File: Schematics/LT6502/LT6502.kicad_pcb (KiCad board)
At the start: 4 copper layers, 261 x 83 mm, 227 parts, among them IC1 ATF1508AS-7AX100, IC2 MP2636GR-P, IC3 W65C22S6TQG-14, J1 Conn_02x05_Odd_Even, J11 Conn_02x04_Odd_Even, J12 Conn_02x06_Odd_Even, J13 Conn_02x06_Odd_Even, J14 KeyConn, J15 Conn_01x06, J16 Conn_01x03, J18 Conn_01x03, J2 USBPD_PROG, J3 USB_C_Receptacle_USB2.0_16P, J4 BATTERY JST PH-2A, J5 Conn_02x20_Odd_Even, J6 USB_C_Receptacle_USB2.0_16P, J7 Conn_01x02, J8 Conn_02x26_Top_Bottom, J9 DIN41612_02x32_AC, Q1 STL9P3LLH6, Q2 IRLML6402, Q3 STL9P3LLH6, U1 TC1232, U10 FT245RNL, U11 LM386, U12 W65C51NxP, U2 W65C02S6TQG-14, U3 IS62C256AL, U4 IS62C256AL, U5 SST39SF010, U6 STUSB4500QTR, U7 AP63203WU, U8 TXS0108, U9 TXS0108, X1 28.322MHz, X2 1.8432MHz, Y1 ECS-P55-28.000MHZ-AN

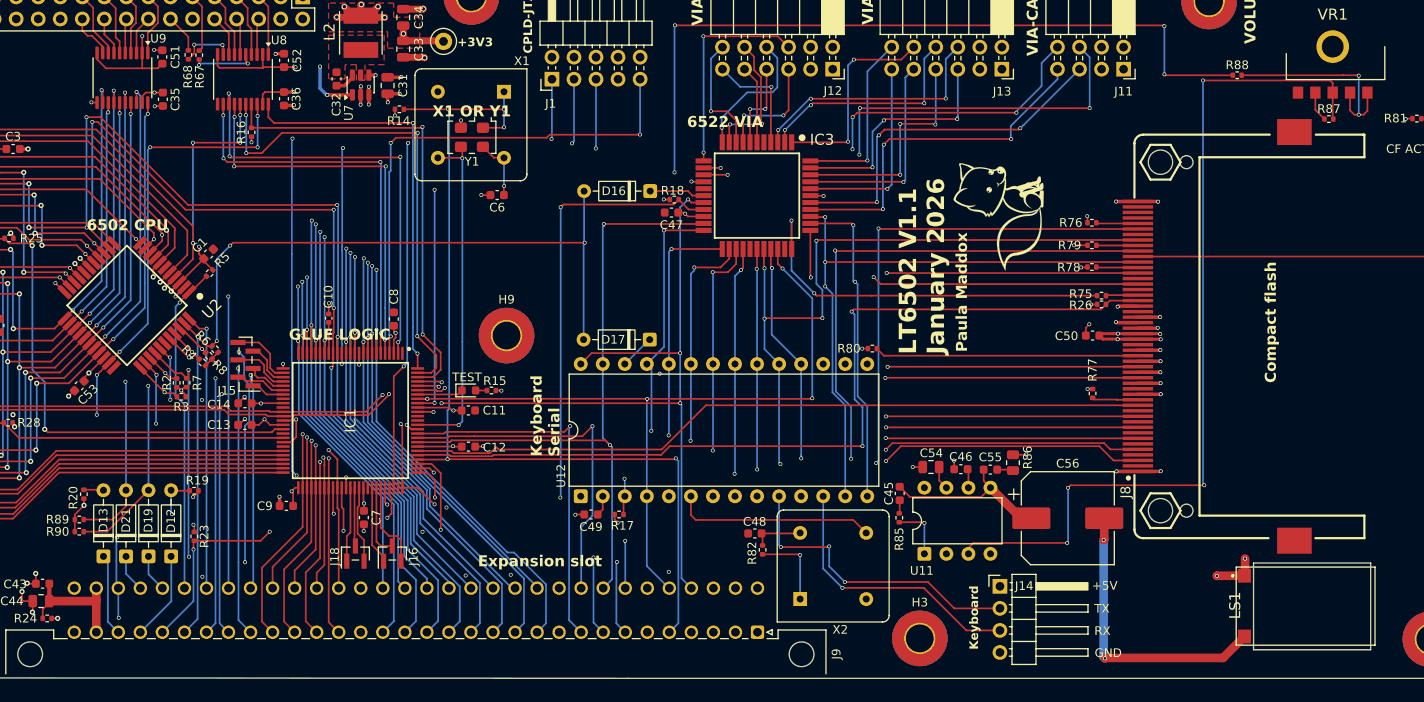
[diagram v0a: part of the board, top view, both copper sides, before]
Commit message: Added enable for TXS0108 on data bus
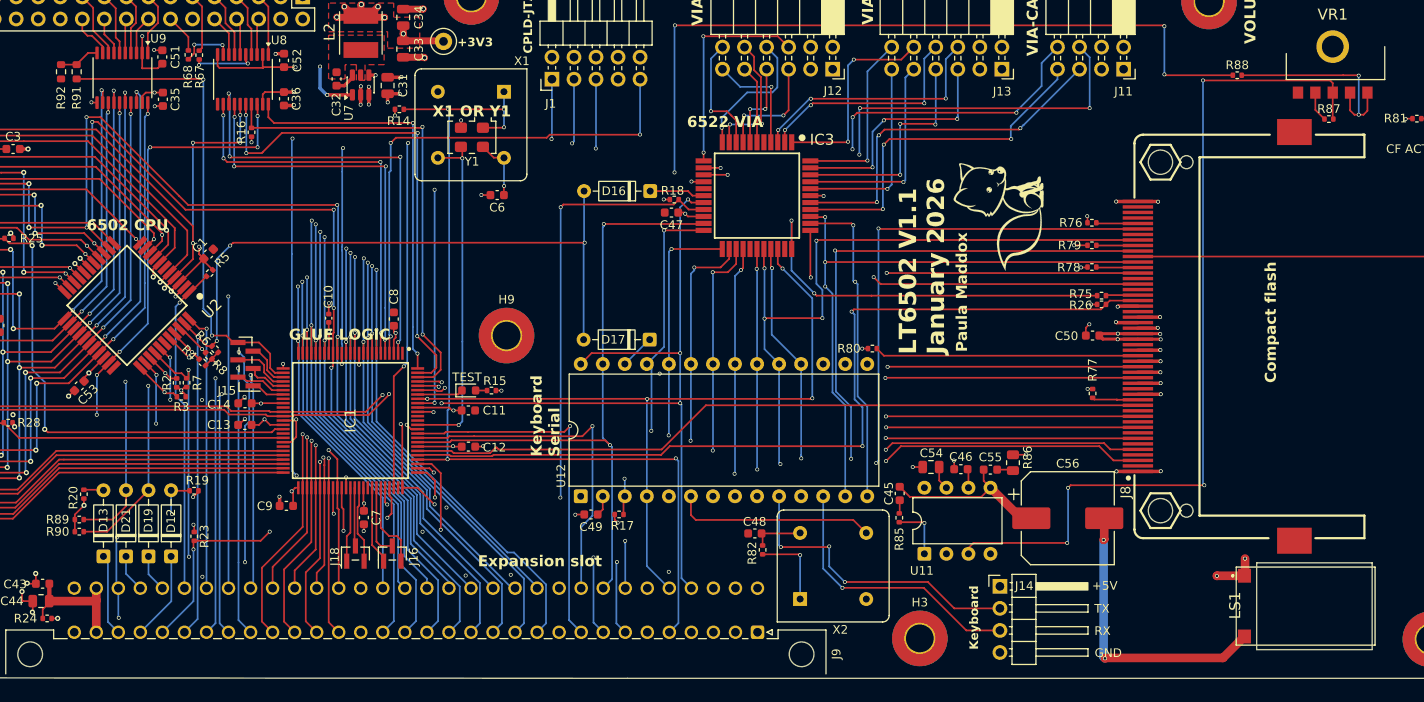
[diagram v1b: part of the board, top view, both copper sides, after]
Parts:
- added R91: 1K8, Resistor_SMD:R_0603_1608Metric, F.Cu at (199.5, 86.1)
- added R92: 3K3, Resistor_SMD:R_0603_1608Metric, F.Cu at (197.7, 86.1)
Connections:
- net Net-(IC1-I/O_20) renamed /Display Connector/DISP_DATA_EN
- U9 pad 10: +3.3V -> Net-(U9-OE)
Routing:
- net /Display Connector/DISP_DATA_EN: track 7.63 -> 54.7 mm, vias 0 -> 2
- net +3.3V: track 101.3 -> 95.0 mm
- net Net-(U9-OE): track 0.00 -> 4.72 mm
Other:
- outline, holes or cut-outs redrawn
